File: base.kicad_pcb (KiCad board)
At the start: 2 copper layers, 95 x 95 mm, 7 parts, among them M8 MountingHole_8.4mm_M8

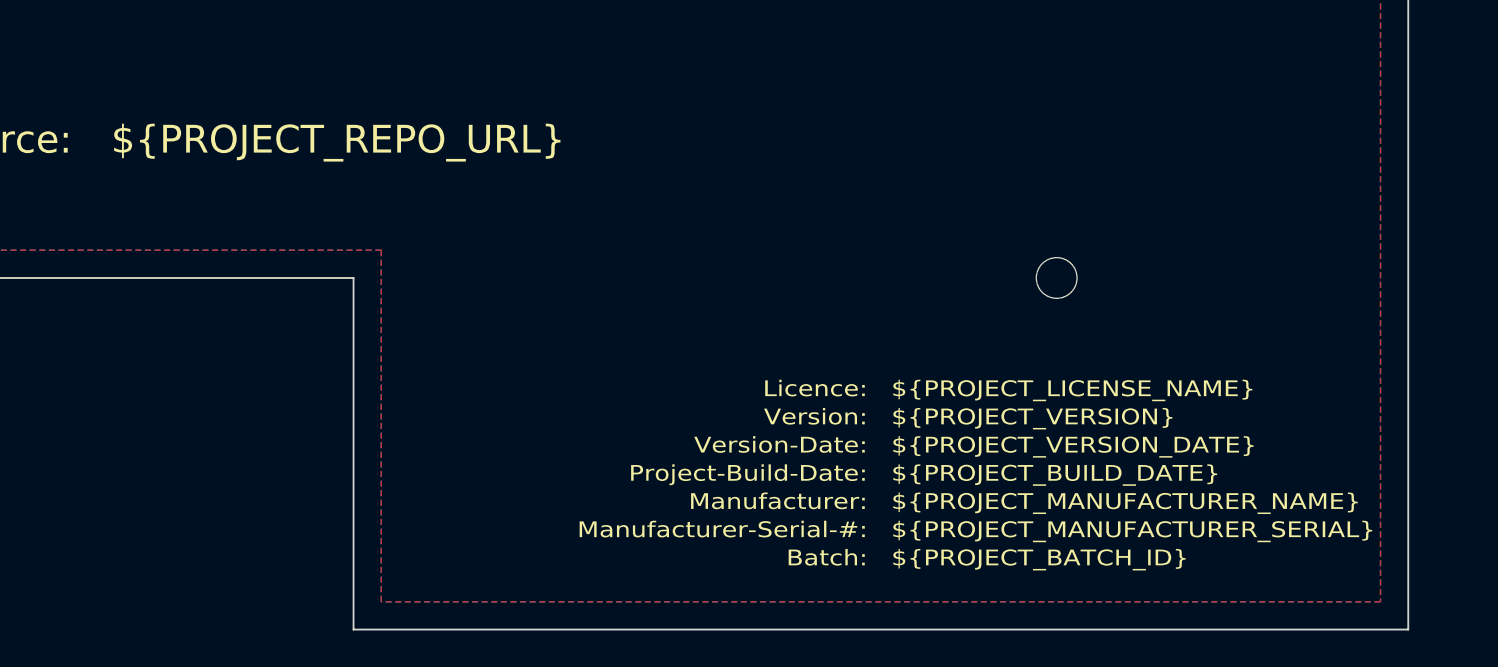
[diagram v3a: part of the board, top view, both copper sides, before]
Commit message: Update PCB with var names form projvar
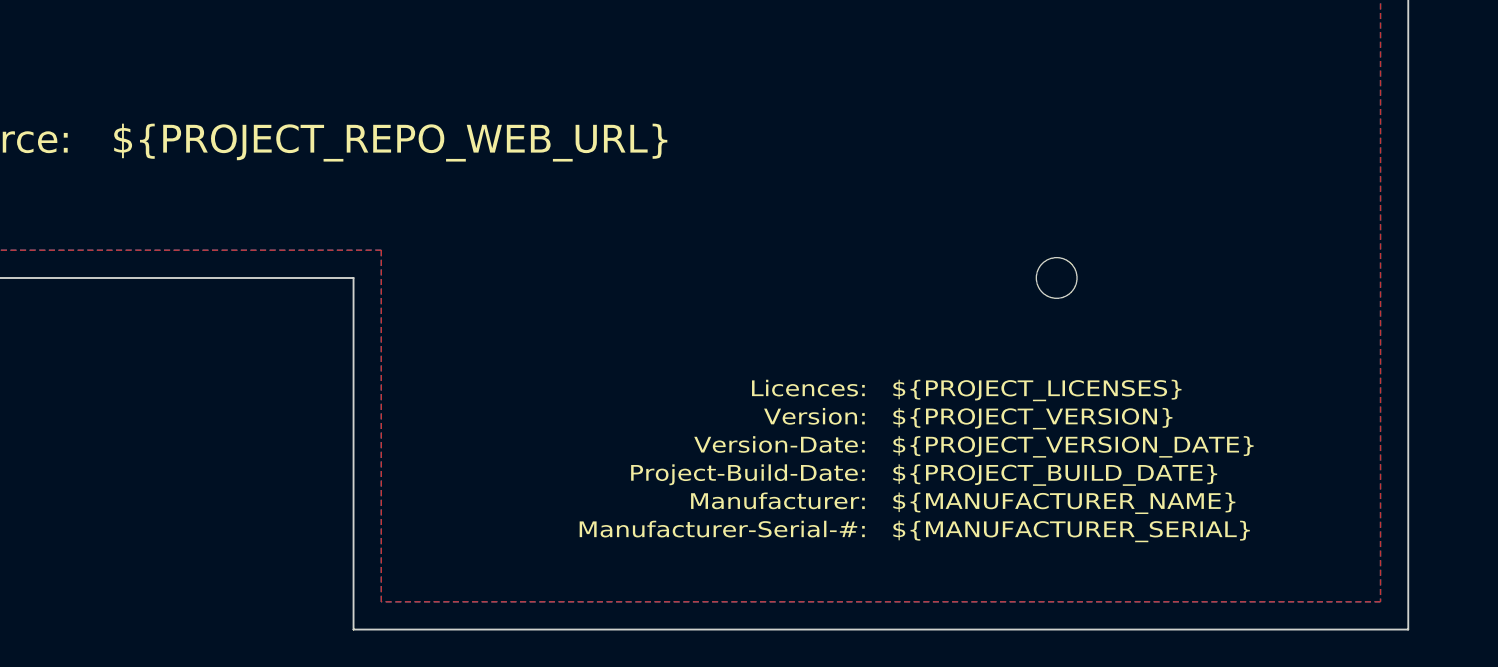
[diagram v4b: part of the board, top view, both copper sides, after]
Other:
- board text added: "${MANUFACTURER_NAME}"
- board text added: "${MANUFACTURER_SERIAL}"
- board text added: "${PROJECT_LICENSES}"
- board text added: "${PROJECT_REPO_WEB_URL}"
- board text added: "Licences:"
- board text removed: "${PROJECT_BATCH_ID}"
- board text removed: "${PROJECT_LICENSE_NAME}"
- board text removed: "${PROJECT_MANUFACTURER_NAME}"
- board text removed: "${PROJECT_MANUFACTURER_SERIAL}"
- board text removed: "${PROJECT_REPO_URL}"
- board text removed: "Batch:"
- board text removed: "Licence:"
